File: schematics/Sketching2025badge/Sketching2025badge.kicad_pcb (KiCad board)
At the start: 2 copper layers, 100 x 100 mm, 20 parts, among them J1 Conn_02x03, J2 Conn_01x04_Pin, U1 ATtiny816-M, U2 BH-AAA-A1AJ001, U3 BH-AAA-A1AJ001

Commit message: almost routed, difficult getting through the maze of the B.Mask
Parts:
- added LED4: SK6812SIDE, todbot_stuff:LED-SMD_4P-L4.0-W1.6-L, B.Cu at (121.6, 119.6)
- added LED5: SK6812SIDE, todbot_stuff:LED-SMD_4P-L4.0-W1.6-L, B.Cu at (75.2, 104.6)
- added LED6: SK6812SIDE, todbot_stuff:LED-SMD_4P-L4.0-W1.6-L, B.Cu at (69.6, 86.0)
- added SW1: Capacitive_Button, todbot_stuff:Pad-CapTouch-10mm-roundrect-nosilk, F.Cu at (81.8, 64.7)
- added SW2: Capacitive_Button, todbot_stuff:Pad-CapTouch-10mm-roundrect-nosilk, F.Cu at (63.8, 104.3)
- added SW3: Capacitive_Button, todbot_stuff:Pad-CapTouch-10mm-roundrect-nosilk, F.Cu at (138.2, 93.0)
- added TP1: Sewable, TestPoint:TestPoint_Keystone_5010-5014_Multipurpose, B.Cu at (59.0, 76.4)
- added TP2: Sewable, TestPoint:TestPoint_Keystone_5010-5014_Multipurpose, B.Cu at (53.4, 100.0)
- added TP3: Sewable, TestPoint:TestPoint_Keystone_5010-5014_Multipurpose, B.Cu at (146.2, 100.0)
- added TP4: Sewable, TestPoint:TestPoint_Keystone_5010-5014_Multipurpose, B.Cu at (140.6, 123.4)
- BAT1: renamed from U2; moved to F.Cu
- BAT2: renamed from U3; moved to F.Cu
- J1: footprint todbot_stuff:Simple_Addon_v2-SAO-2x3-minimal -> Connector_PinSocket_2.54mm:PinSocket_2x03_P2.54mm_Vertical
- moved BAT2 146.7 mm to (86.2, 128.9), turned to -25.6 degrees
- moved R4 142.2 mm to (76.5, 71.0), turned to 180 degrees
- moved R5 134.3 mm to (70.0, 111.0)
- moved D1 102.5 mm to (100.0, 66.4)
- moved R9 102.1 mm to (107.4, 108.4), turned to 0 degrees
- moved R8 101.2 mm to (100.0, 70.6)
- moved C1 100.3 mm to (109.5, 125.9)
- moved C2 100.3 mm to (109.5, 122.4)
- moved U1 100.3 mm to (100.0, 123.4)
- moved J2 100.2 mm to (100.0, 144.1), turned to -90 degrees
- moved LED1 100.0 mm to (103.5, 93.6)
- moved LED2 100.0 mm to (93.0, 99.7)
- moved LED3 100.0 mm to (103.5, 105.8)
- moved R3 90.5 mm to (109.3, 130.0)
- moved R7 85.9 mm to (109.3, 132.4), turned to 180 degrees
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- renumbered LED3 to LED2, LED2 to LED3
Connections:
- net Net-(J2-Pin_4) renamed /TX
- BAT1 pad 2: unconnected-(U2-+-Pad2) -> VCC
- J1 pad 1: unconnected-(J1-+12V-Pad1) -> VCC
- J1 pad 2: unconnected-(J1-+12V-Pad2) -> GND
- J1 pad 3: unconnected-(J1-GND-Pad3) -> /SDA
- J1 pad 4: unconnected-(J1-GND-Pad4) -> /SCL
- J1 pad 5: unconnected-(J1-GND-Pad5) -> /TXD
- J1 pad 6: unconnected-(J1-GND-Pad6) -> /RXD
- LED3 pad 3: unconnected-(LED2-DOUT-Pad3) -> Net-(LED3-DOUT)
- U1 pad 2: unconnected-(U1-PA3-Pad2) -> /PA3
- U1 pad 8: unconnected-(U1-PA7-Pad8) -> /PA7
- U1 pad 9: unconnected-(U1-PB5-Pad9) -> /PB5
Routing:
- net GND: track 0.00 -> 302.8 mm, vias 0 -> 9
- net VCC: track 0.00 -> 259.1 mm, vias 0 -> 4
- net /TOUCH0: track 0.00 -> 96.0 mm, vias 0 -> 1
- net /TXD: track 0.00 -> 88.5 mm, vias 0 -> 1
- net Net-(BAT1--): track 0.00 -> 74.1 mm, vias 0 -> 1
- net /RXD: track 0.00 -> 67.5 mm, vias 0 -> 2
- net /TOUCH1: track 0.00 -> 64.7 mm, vias 0 -> 3
- net /SDA: track 0.00 -> 60.9 mm, vias 0 -> 2
- net /SCL: track 0.00 -> 60.8 mm, vias 0 -> 2
- net /TOUCH2: track 0.00 -> 60.1 mm, vias 0 -> 2
- net /LED: track 0.00 -> 54.1 mm, vias 0 -> 1
- net Net-(LED3-DOUT): track 0.00 -> 28.8 mm
- net /RESET: track 0.00 -> 27.7 mm, vias 0 -> 2
- net /LED_DAT: track 0.00 -> 20.3 mm, vias 0 -> 2
- net Net-(LED2-DOUT): track 0.00 -> 19.9 mm
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- removed copper zone on F.Cu, net GND
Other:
- board text added: "rx scl gnd"
- board text added: "tx rx 3v3 gnd"
- board text added: "tx sda 3v3"
- board text removed: "tx rx"
- board text removed: "tx rx v+ gnd"

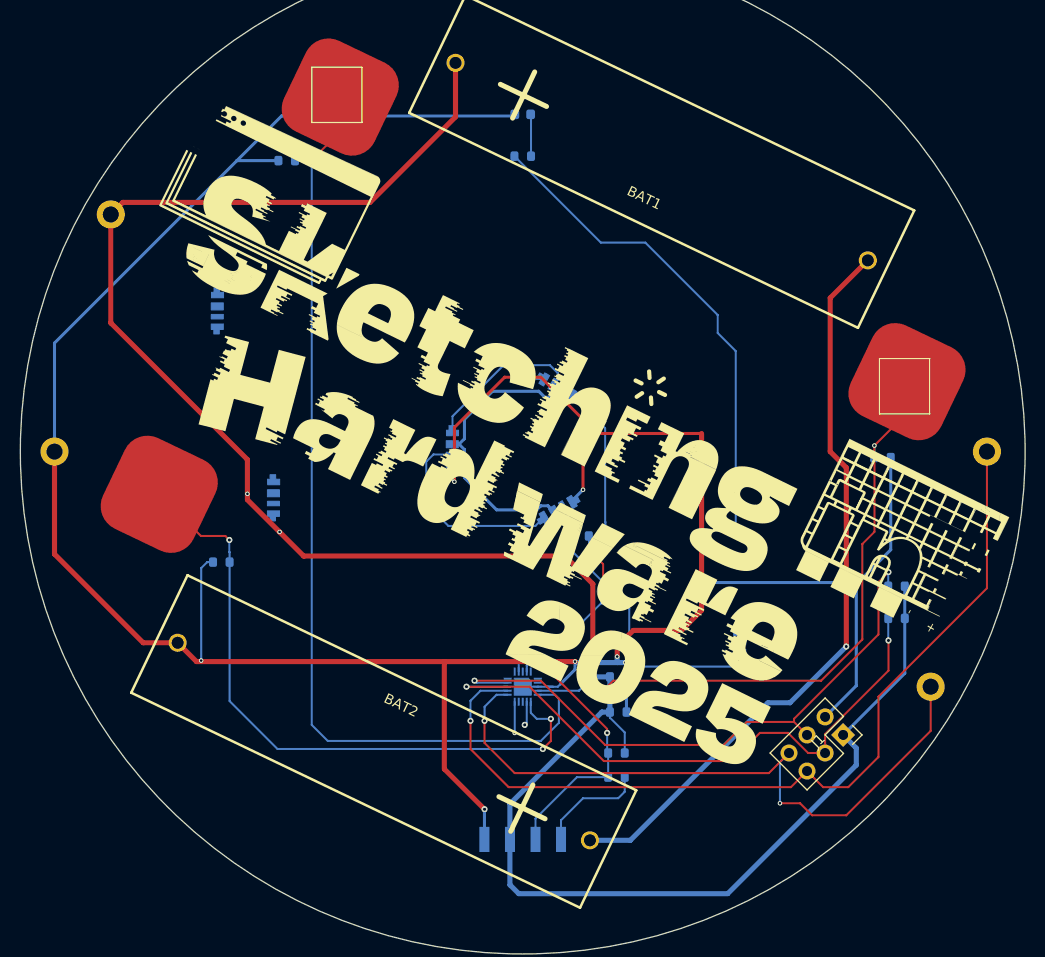
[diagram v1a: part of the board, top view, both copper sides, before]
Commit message: first version routed, not pass drc yet
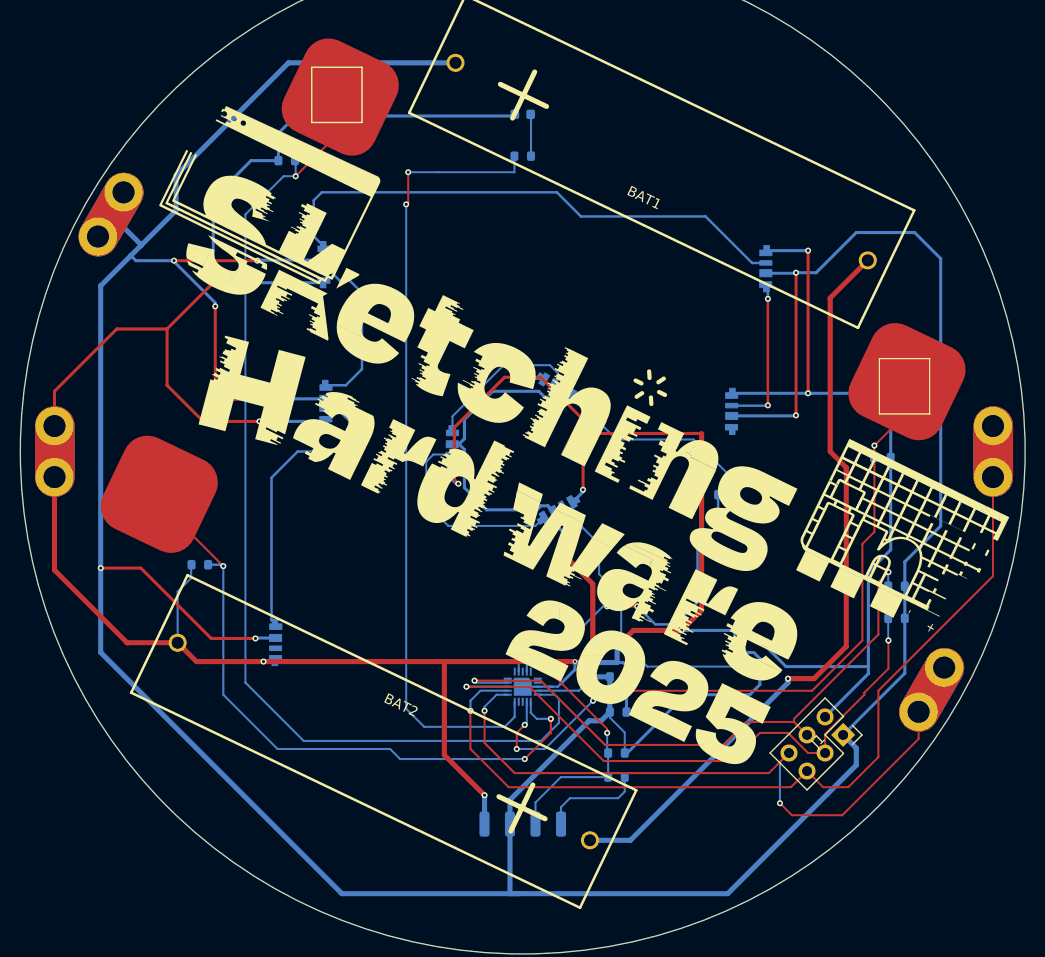
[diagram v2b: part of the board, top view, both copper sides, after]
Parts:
- removed TP4: Sewable, TestPoint:TestPoint_Keystone_5010-5014_Multipurpose
- added LED7: SK6812SIDE, todbot_stuff:LED-SMD_4P-L4.0-W1.6-L, B.Cu at (80.2, 81.4)
- added LED8: SK6812SIDE, todbot_stuff:LED-SMD_4P-L4.0-W1.6-L, B.Cu at (80.4, 95.2)
- added LED9: SK6812SIDE, todbot_stuff:LED-SMD_4P-L4.0-W1.6-L, B.Cu at (75.4, 119.0)
- added TP5: Sewable, todbot_stuff:Lilypad-BUTTONHOLE, B.Cu at (140.7, 123.7)
- TP1, TP2, TP3: footprint TestPoint:TestPoint_Keystone_5010-5014_Multipurpose -> todbot_stuff:Lilypad-BUTTONHOLE
- moved LED6 54.7 mm to (124.2, 81.8), turned to 90 degrees
- moved LED5 46.4 mm to (120.8, 96.0), turned to 90 degrees
- moved R9 13.5 mm to (120.3, 104.3)
- moved R5 2.15 mm to (67.9, 111.3)
- moved J2 1.53 mm to (100.0, 142.6)
- moved TP3 0.60 mm to (146.8, 100.0), turned to 90 degrees
- turned TP1 to 60 degrees
- turned TP2 to 90 degrees
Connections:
- LED6 pad 3: unconnected-(LED6-DOUT-Pad3) -> Net-(LED6-DOUT)
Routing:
- net VCC: track 259.1 -> 448.7 mm, vias 4 -> 10
- net GND: track 302.8 -> 374.0 mm, vias 9 -> 13
- net Net-(LED6-DOUT): track 0.00 -> 53.3 mm
- net Net-(LED8-DOUT): track 0.00 -> 30.1 mm
- net /LED: track 54.1 -> 79.1 mm, vias 1 -> 2
- net Net-(LED7-DOUT): track 0.00 -> 16.6 mm
- net Net-(LED5-DOUT): track 0.00 -> 15.5 mm, vias 0 -> 2
- net /LED_DAT: track 20.3 -> 35.3 mm
- net /TOUCH2: track 60.1 -> 72.8 mm, vias 2 -> 4
- net /TOUCH0: track 96.0 -> 103.5 mm
- net Net-(LED1-DIN): track 15.2 -> 20.9 mm
- net /RXD: track 67.5 -> 64.3 mm
- net /TXD: track 88.5 -> 86.2 mm
- net /TX: track 10.9 -> 10.1 mm
- net /RESET: track 27.7 -> 27.1 mm
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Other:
- board text removed: "uart"

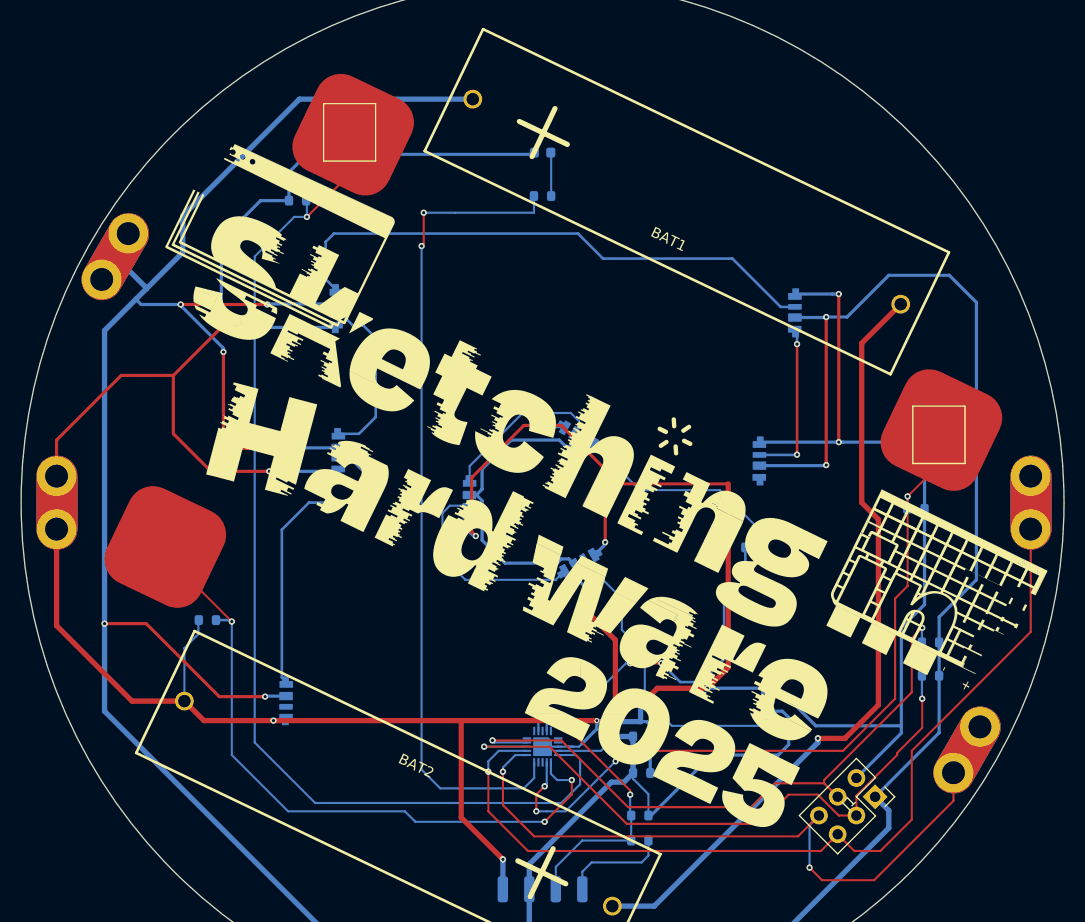
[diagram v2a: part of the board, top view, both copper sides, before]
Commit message: routed, mostly pass drc
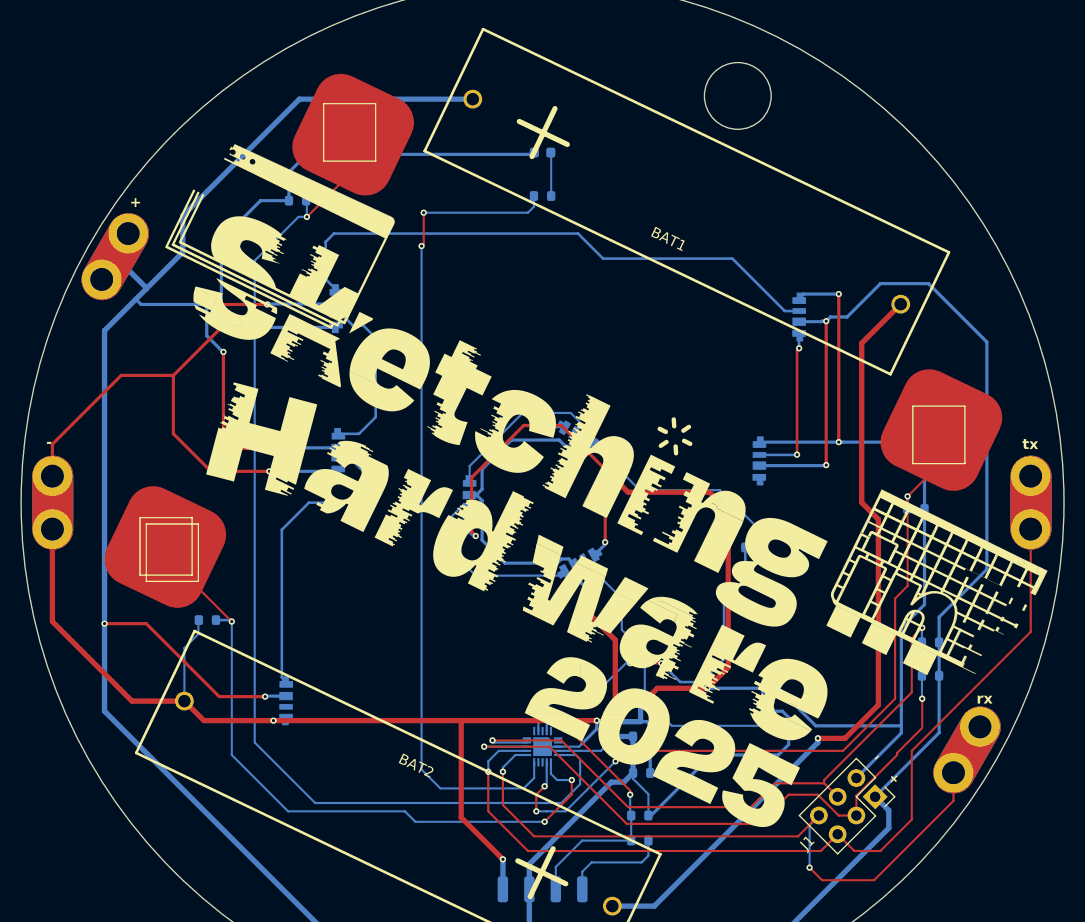
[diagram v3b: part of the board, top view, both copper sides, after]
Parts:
- added H1: MountingHole, MountingHole:MountingHole_6.4mm_M6, F.Cu at (118.7, 61.0)
- moved LED6 0.57 mm to (124.6, 82.2)
- moved TP2 0.40 mm to (53.0, 100.0)
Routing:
- net VCC: track 448.7 -> 445.3 mm
- net Net-(LED2-DOUT): track 19.9 -> 17.5 mm
- net GND: track 374.0 -> 372.6 mm
- net Net-(LED6-DOUT): track 53.3 -> 53.8 mm
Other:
- board text added: "+"
- board text added: "-"
- board text added: "21 Aug 2025 - @todbot & @leeborg github.com/todbot/Sketching2025badge"
- board text added: "rx"
- board text added: "tx"
- board text removed: "16 Aug 2025 - @todbot & @leeborg github.com/todbot/Sketching2025badge"

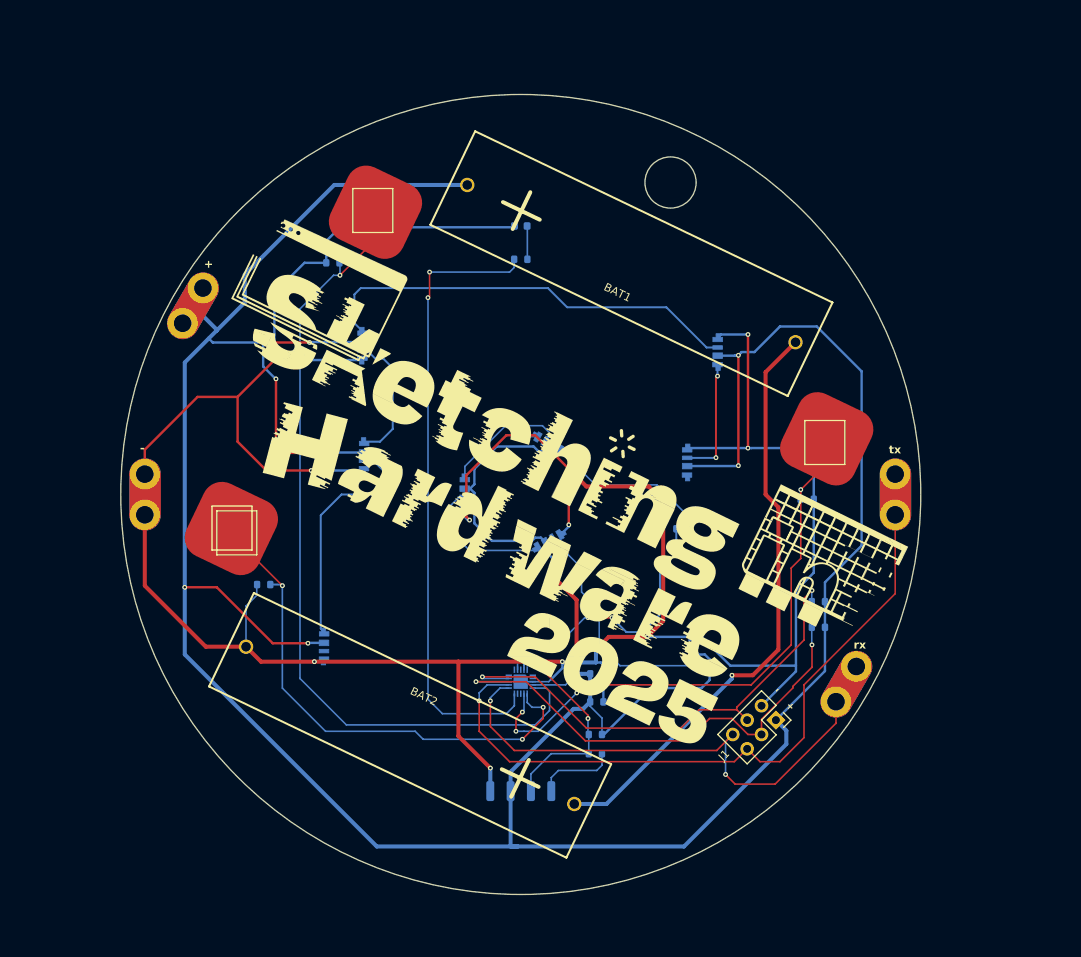
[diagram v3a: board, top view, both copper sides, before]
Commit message: added bypass caps and switch
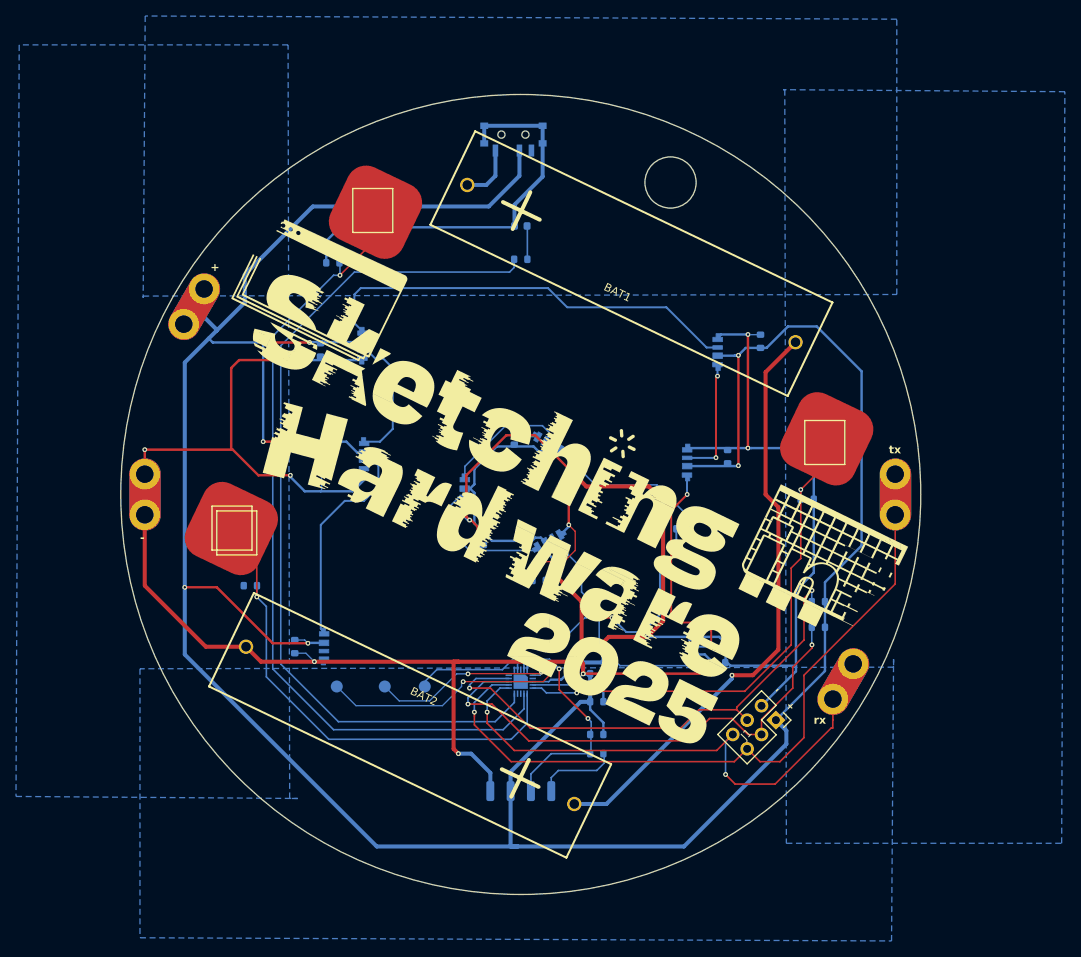
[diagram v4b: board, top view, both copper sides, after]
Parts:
- removed TP5: Sewable, todbot_stuff:Lilypad-BUTTONHOLE
- added C10: 100n, Resistor_SMD:R_0603_1608Metric, B.Cu at (75.1, 94.4)
- added C11: 100n, Resistor_SMD:R_0603_1608Metric, B.Cu at (71.7, 119.0)
- added C3: 100n, Resistor_SMD:R_0603_1608Metric, B.Cu at (99.2, 92.9)
- added C4: 100n, Resistor_SMD:R_0603_1608Metric, B.Cu at (95.3, 105.5)
- added C5: 100n, Resistor_SMD:R_0603_1608Metric, B.Cu at (102.3, 110.7)
- added C6: 100n, Resistor_SMD:R_0603_1608Metric, B.Cu at (124.7, 121.0)
- added C7: 100n, Resistor_SMD:R_0603_1608Metric, B.Cu at (125.9, 95.3)
- added C8: 100n, Resistor_SMD:R_0603_1608Metric, B.Cu at (130.0, 80.9)
- added C9: 100n, Resistor_SMD:R_0603_1608Metric, B.Cu at (75.0, 81.9)
- added SW10: SSSS811101, easyeda2kicad:SW-SMD_SSSS811101, B.Cu at (99.1, 55.5)
- added TP4: Sewable, todbot_stuff:Lilypad-BUTTONHOLE, B.Cu at (140.3, 123.4)
- added TP6: TestPoint, TestPoint:TestPoint_Pad_D1.5mm, B.Cu at (88.0, 124.0)
- added TP7: TestPoint, TestPoint:TestPoint_Pad_D1.5mm, B.Cu at (77.0, 124.0)
- added TP8: TestPoint, TestPoint:TestPoint_Pad_D1.5mm, B.Cu at (83.0, 124.0)
- moved R5 1.67 mm to (66.2, 111.4)
- moved TP1 0.19 mm to (59.1, 76.5)
- moved R3 0.17 mm to (109.5, 130.0)
- moved R7 0.17 mm to (109.5, 132.4)
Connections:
- BAT1 pad 2: VCC -> Net-(BAT1-+)
- U1 pad 5: /TOUCH0 -> /TOUCH2
- U1 pad 7: /TOUCH2 -> /TOUCH0
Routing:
- net GND: track 372.6 -> 408.0 mm, vias 13 -> 15
- net /SDA_ALT: track 0.00 -> 33.6 mm, vias 0 -> 2
- net /LED: track 78.8 -> 108.3 mm, vias 2 -> 0
- net Net-(LED4-DOUT): track 0.00 -> 28.0 mm, vias 0 -> 2
- net /SCL_ALT: track 0.00 -> 23.2 mm, vias 0 -> 2
- net /LED_DAT: track 35.3 -> 49.4 mm
- net VCC: track 445.3 -> 458.6 mm, vias 10 -> 11
- net /TOUCH2: track 72.8 -> 63.9 mm, vias 4 -> 2
- net Net-(BAT1-+): track 0.00 -> 7.15 mm
- net /SCL: track 60.8 -> 64.1 mm
- net /TOUCH1: track 65.2 -> 62.1 mm, vias 3 -> 1
- net Net-(LED8-DOUT): track 30.1 -> 27.4 mm
- net /SDA: track 60.9 -> 63.3 mm
- net /RESET: track 27.1 -> 28.6 mm
- net /TOUCH0: track 103.3 -> 102.0 mm
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- added copper zone on B.Cu, net GND
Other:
- board text added: "off on"

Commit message: verify jlc test run1
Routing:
- net GND: track 408.0 -> 407.3 mm
- net Net-(LED8-DOUT): track 27.4 -> 26.9 mm
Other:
- board text added: "29 Aug 2025 - @todbot & @leeborg github.com/todbot/Sketching2025badge"
- board text removed: "21 Aug 2025 - @todbot & @leeborg github.com/todbot/Sketching2025badge"
